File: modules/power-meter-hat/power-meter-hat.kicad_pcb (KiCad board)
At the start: 2 copper layers, 65 x 56 mm, 45 parts, among them J1 GPIO, J2 Barrel_Jack_Switch, J3 Conn_01x02, J4 Conn_01x02, J5 Conn_01x02, U1 CAT24C256, U2 NCP1117-3.3_SOT223, U3 INA219AxD, U4 INA219AxD, U5 INA219AxD

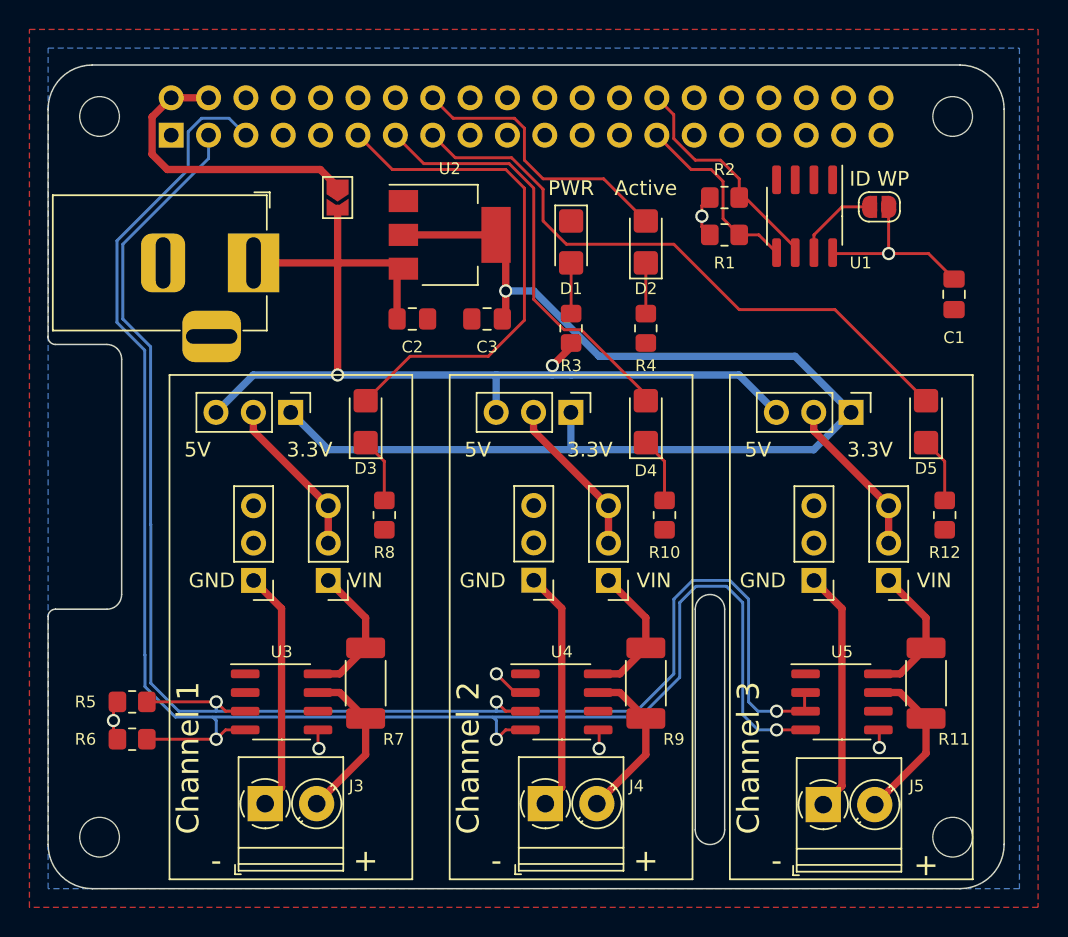
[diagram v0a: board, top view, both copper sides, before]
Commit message: Move jumpers to bottom side & other improvements
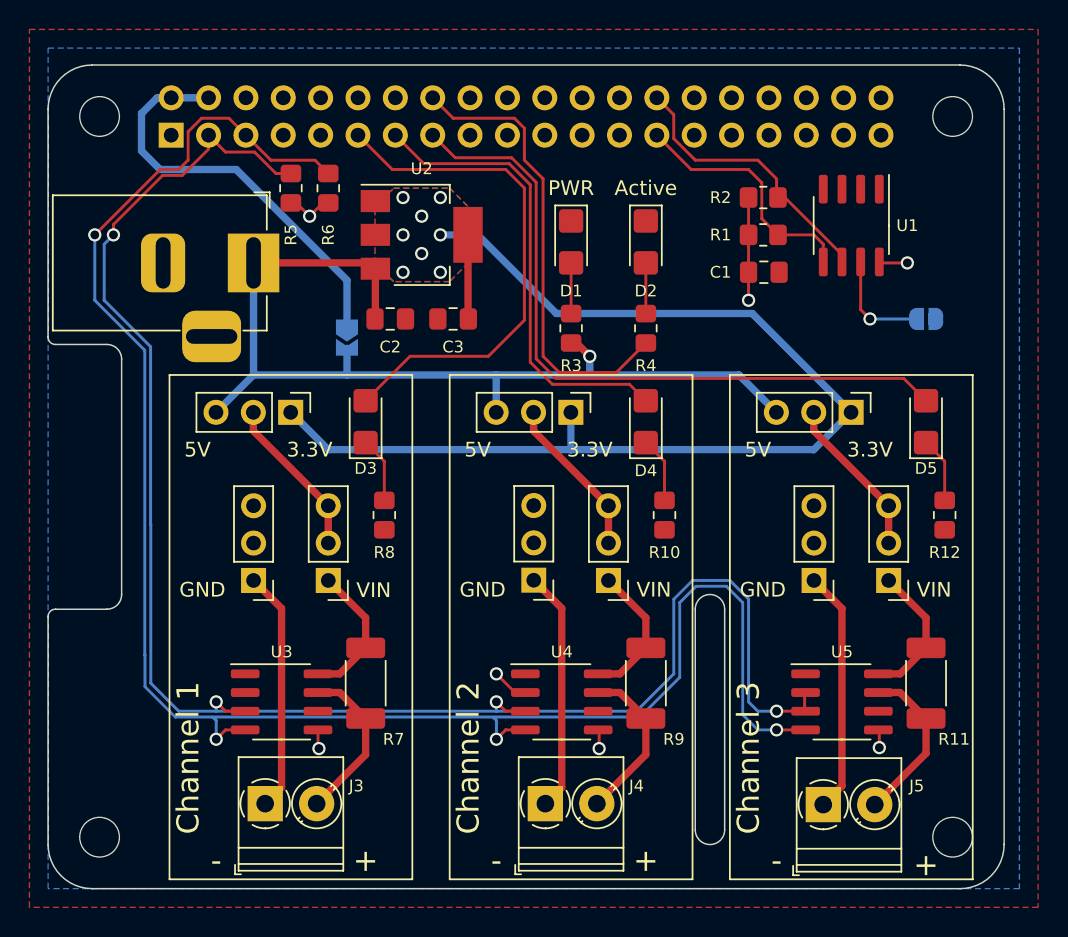
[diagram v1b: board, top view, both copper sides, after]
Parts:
- JP1, JP2: moved to B.Cu
- moved R6 39.8 mm to (119.0, 52.4), turned to 90 degrees
- moved R5 36.6 mm to (116.5, 52.4), turned to 90 degrees
- moved C1 13.0 mm to (148.7, 58.1), turned to 0 degrees
- moved JP2 9.55 mm to (120.3, 62.5)
- moved JP1 8.26 mm to (159.7, 61.3)
- moved U1 3.24 mm to (154.6, 54.9)
- moved R1 2.63 mm to (148.6, 55.5)
- moved R2 2.63 mm to (148.6, 53.0)
- moved C3 2.31 mm to (127.5, 61.3)
- moved U2 1.91 mm to (125.4, 55.5)
- moved C2 1.50 mm to (123.3, 61.3)
- turned D2 to -90 degrees
- turned R4 to -90 degrees
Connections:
- D2 pad 1: Net-(D2-Pad1) -> GND
- D2 pad 2: /GPIO[23] -> Net-(R4-Pad1)
- R4 pad 1: GND -> Net-(R4-Pad1)
- R4 pad 2: Net-(D2-Pad1) -> /GPIO[23]
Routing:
- net /GPIO[23]: track 19.2 -> 31.4 mm
- net +5V: track 20.4 -> 28.3 mm
- net /GPIO[22]: track 42.3 -> 48.0 mm
- net +3V3: track 24.1 -> 18.4 mm
- net /ID_SDA: track 12.9 -> 17.0 mm
- net /SCL: track 118.6 -> 122.6 mm, vias 3 -> 4
- net /SDA: track 111.9 -> 115.7 mm, vias 3 -> 4
- net +5VP: track 70.7 -> 67.0 mm, vias 2 -> 1
- net /ID_SCL: track 15.7 -> 19.2 mm
- net Net-(R4-Pad1): track 0.00 -> 3.45 mm
- net Net-(D2-Pad1): track 3.45 -> 0.00 mm
- net /GPIO[27]: track 29.2 -> 31.6 mm
- net Net-(JP1-Pad1): track 5.79 -> 7.31 mm, vias 0 -> 1
- net +3.3VP: track 82.0 -> 81.4 mm, vias 1 -> 8
- added copper zone on B.Cu, net +3.3VP
- added copper zone on F.Cu, net +3.3VP

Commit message: Add test points for SDA/SCL/GND
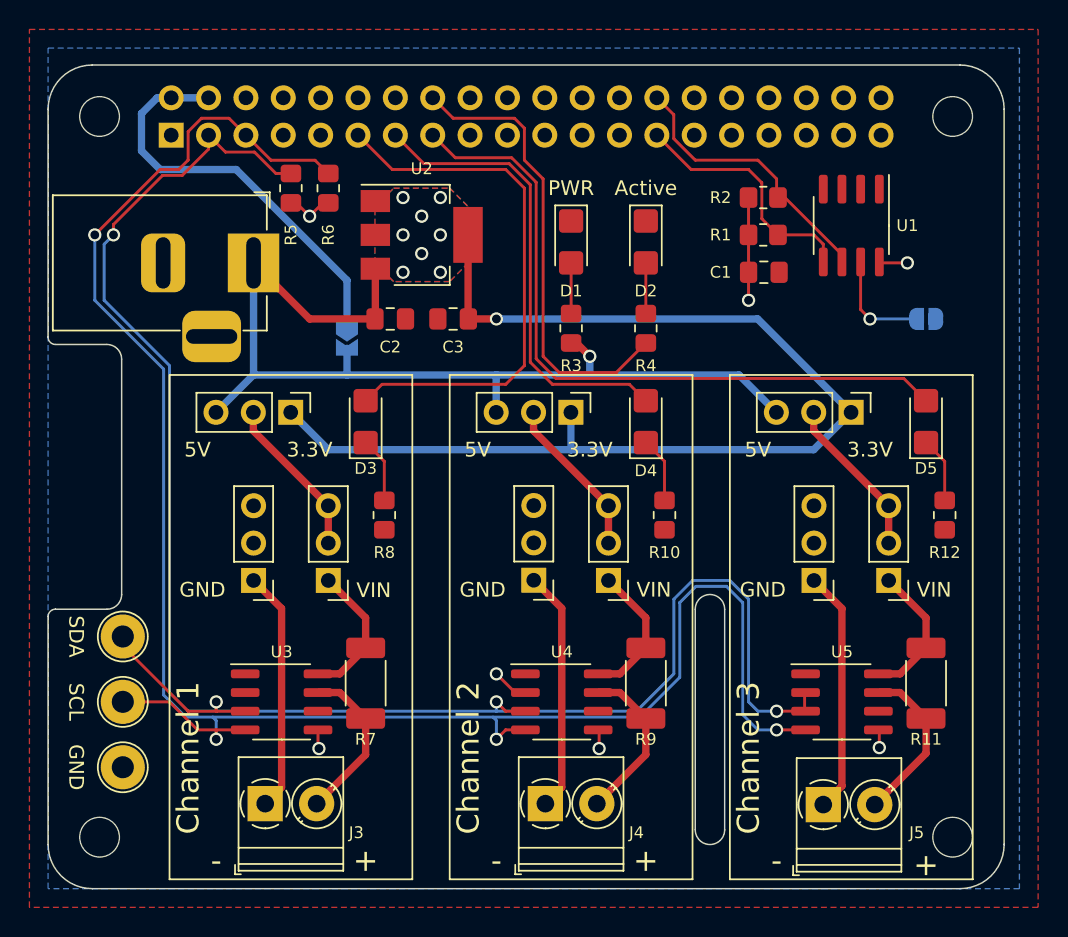
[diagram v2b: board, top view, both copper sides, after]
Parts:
- added TP1: TestPoint, TestPoint:TestPoint_Loop_D2.54mm_Drill1.5mm_Beaded, F.Cu at (105.1, 91.7)
- added TP2: TestPoint, TestPoint:TestPoint_Loop_D2.54mm_Drill1.5mm_Beaded, F.Cu at (105.1, 82.9)
- added TP3: TestPoint, TestPoint:TestPoint_Loop_D2.54mm_Drill1.5mm_Beaded, F.Cu at (105.1, 87.3)
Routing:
- net /SDA: track 115.7 -> 124.5 mm
- net /SCL: track 122.6 -> 129.7 mm
- net +3.3VP: track 81.4 -> 77.1 mm, vias 8 -> 9
- net /GPIO[17]: track 34.8 -> 36.7 mm
- net +5VP: track 67.0 -> 68.4 mm
